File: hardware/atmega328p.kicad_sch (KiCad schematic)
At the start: 27 parts, among them J401 USART, J402 Conn_01x02_Socket, U401 ATmega328-P, Y401 16MHz

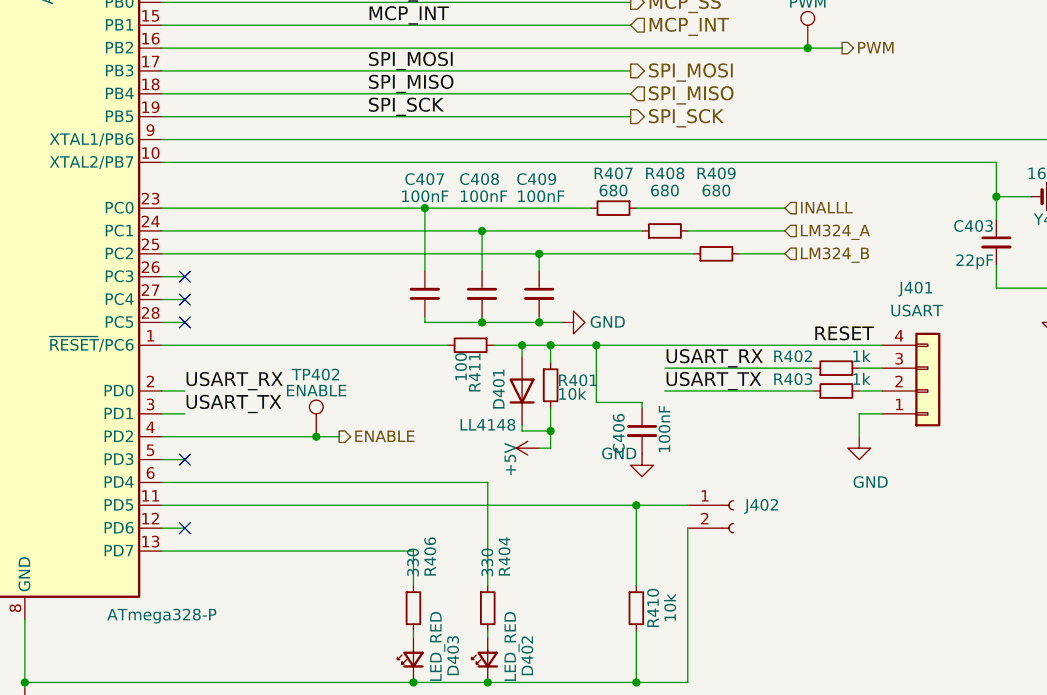
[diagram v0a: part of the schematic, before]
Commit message: Schematic organization improvement, use <driver> sheet as example
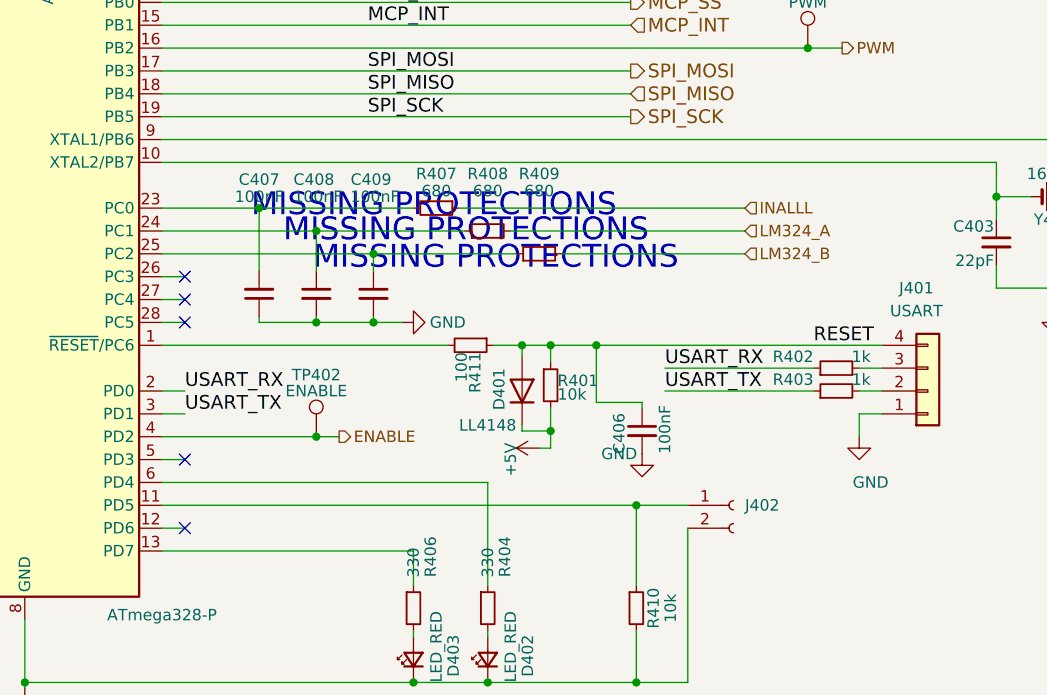
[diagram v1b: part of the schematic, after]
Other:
- note added: "MISSING PROTECTIONS"
- moved on the sheet: C407, C408, C409, R407, R408, R409

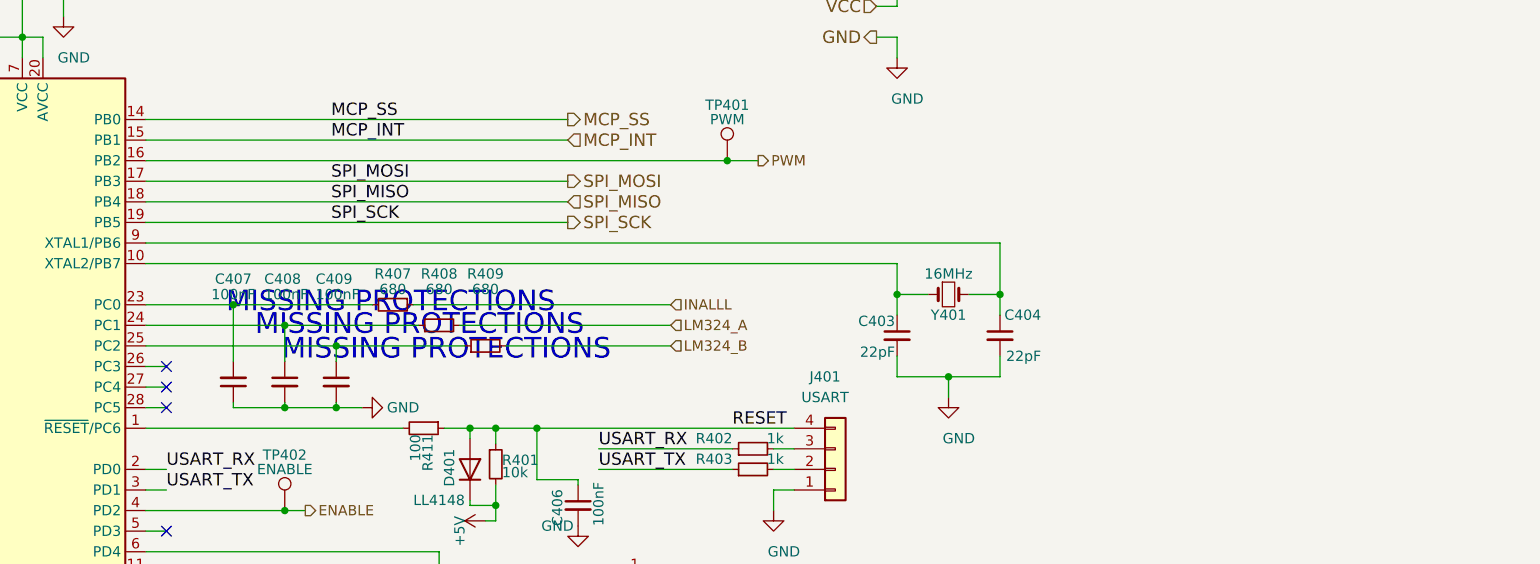
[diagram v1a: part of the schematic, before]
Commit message: add diode protections for Vsense OpAmps and uC port
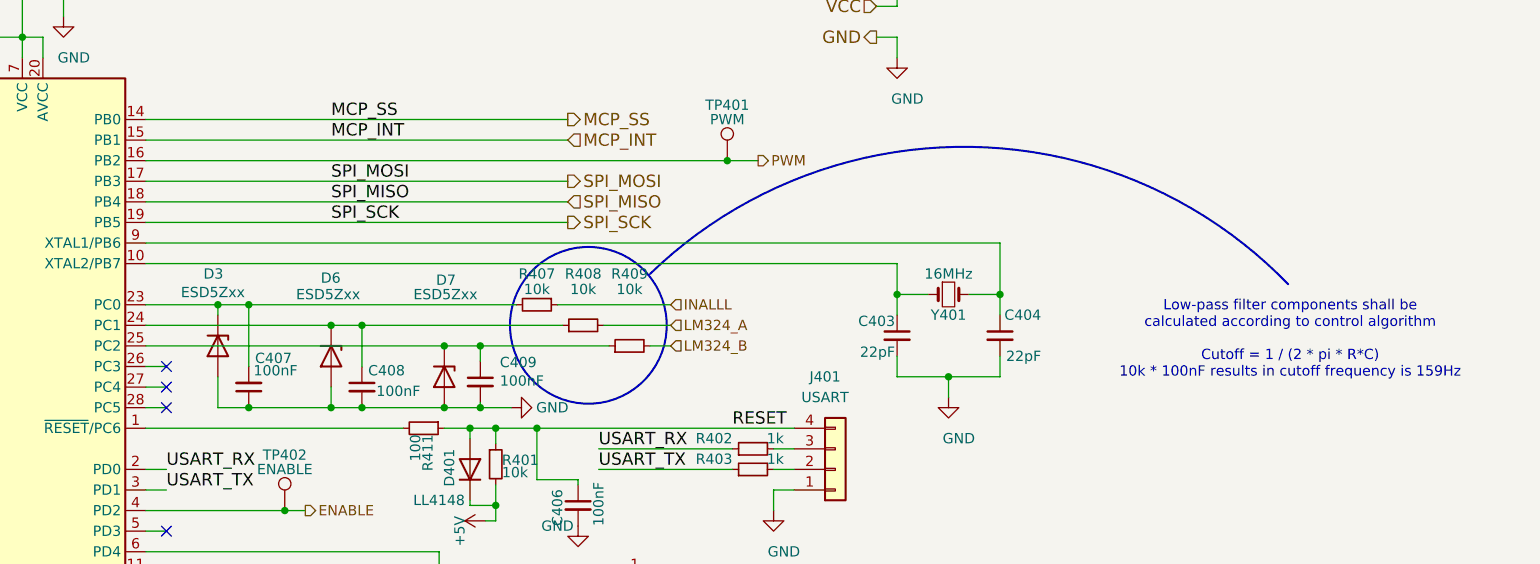
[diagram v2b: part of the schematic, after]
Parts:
- added D3, D6, D7: ESD5Zxx, Diode_SMD:D_SOD-523, symbol Diode:ESD5Zxx
- R407, R408, R409: value 680 -> 10k
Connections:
- net GND: now also D3.2 (A), D6.2 (A), D7.2 (A)
- net at C407.2, R407.2, U401.23 (PC0): now also D3.1 (K)
- net at C408.1, R408.1, U401.24 (PC1): now also D6.1 (K)
- net at C409.1, R409.1, U401.25 (PC2): now also D7.1 (K)
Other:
- note added: "Low-pass filter components shall be calculated according to control algorithm Cutoff = 1 / (2 * pi * R*C) 10k * 100nF results in cutoff frequency is 159Hz"
- note removed: "MISSING PROTECTIONS"
- moved on the sheet: C407, C408, C409, R407, R408, R409
